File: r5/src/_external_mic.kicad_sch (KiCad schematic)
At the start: 132 parts, among them Q12 BSS84PW, Q13 BSS84PW, Q14 NX3008NBKW, Q15 NX3008NBKW, Q16 NX3008NBKW, Q17 NX3008NBKW, Q18 NX3008NBKW, Q19 NX3008NBKW, Q20 BSS84PW, Q21 BSS84PW, Q22 NX3008NBKW, Q23 NX3008NBKW, Q24 NX3008NBKW, Q25 BSS84PW, T18 , T19 , T20 , T23 , T24 , T25 , T26 , T27 , T28 , T29 , T30 , T31 , T32 , T33 , T34 , T35 , T37 , T38 , T43 , T44 , T45 , T46 , T47 , T48 , T49 , T50 , U17 74HC20, U18 THAT5173, U19 74HC74, U20 74HC132, U21 74HC4520, U22 74HC132, U23 THAT1580, U24 74HC688, U25 LM4562, U26 74HC688, U27 AD4005

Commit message: Updates to +/-15V supply. Additional output capacitance. Change to smaller inductor packages. Add 0R links to permit isolation of output. Mods to compensation network. Set feedback resistors to datasheet values.
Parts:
- renumbered C57 to C100, C82 to C101, C52 to C102, C27 to C103, C46 to C104, C47 to C105, C49 to C106, C50 to C107, C60 to C108, C54 to C109, C55 to C110, C84 to C111, C56 to C112, C58 to C113, C59 to C114, C62 to C115, C63 to C116, C64 to C117, C66 to C118, C65 to C119, C67 to C120, C68 to C121, C69 to C122, C70 to C123, C71 to C124, C72 to C125, C73 to C126, C74 to C127, C75 to C128, C76 to C129, C77 to C130, C78 to C131, C79 to C132, C25 to C95, C48 to C96, C53 to C97, C83 to C98, C81 to C99, D15 to D19, D8 to D20, D10 to D21, D11 to D22, D12 to D23, D14 to D24, D13 to D25, Q17 to Q14, Q18 to Q15, Q19 to Q16, Q20 to Q17, Q21 to Q18, Q15 to Q19, Q16 to Q20, Q14 to Q21, Q12 to Q22, Q13 to Q23, Q22 to Q24, Q23 to Q25, Q24 to Q26, Q25 to Q27, R71 to R100, R100 to R101, R79 to R67, R82 to R68, R84 to R69, R85 to R70, R73 to R71, R68 to R72, R74 to R73, R65 to R74, R72 to R75, R64 to R76, R66 to R77, R67 to R78, R47 to R79, R48 to R80, R49 to R82, R50 to R83, R51 to R84, R52 to R85, R55 to R87, R53 to R88, R54 to R89, R56 to R90, R57 to R91, R58 to R92, R59 to R93, R60 to R94, R61 to R95, R62 to R96, R63 to R97, R70 to R98, R69 to R99, T20 to T26, T19 to T27, T18 to T28, T37 to T29, T38 to T30, T44 to T31, T45 to T32, T46 to T33, T23 to T34, T24 to T35, T47 to T36, T43 to T37, T25 to T38, T26 to T39, T48 to T40, T27 to T41, T28 to T42, T29 to T43, T30 to T44, T31 to T45, T49 to T46, T32 to T47, T33 to T48, T50 to T49, T35 to T50, T34 to T51, U17 to U25, U19 to U26, U20 to U27, U22 to U28, U18 to U29, U21 to U30, U23 to U31, U24 to U32, U25 to U33, U26 to U34, U27 to U35

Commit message: Fix broken component annotation by importing back from PCB and fixing duplicates.
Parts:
- Q14: renamed from Q21; value NX3008NBKW -> NX6008NBKW
- renumbered C95 to C25, C103 to C27, C104 to C46, C105 to C47, C96 to C48, C106 to C49, C107 to C50, C102 to C52, C97 to C53, C109 to C54, C110 to C55, C112 to C56, C100 to C57, C113 to C58, C114 to C59, C108 to C60, C115 to C62, C116 to C63, C117 to C64, C119 to C65, C118 to C66, C120 to C67, C121 to C68, C122 to C69, C123 to C70, C124 to C71, C125 to C72, C126 to C73, C127 to C74, C128 to C75, C129 to C76, C130 to C77, C131 to C78, C132 to C79, C99 to C81, C101 to C82, C98 to C83, C111 to C84, D21 to D10, D22 to D11, D23 to D12, D25 to D13, D24 to D14, D19 to D15, D20 to D8, Q22 to Q12, Q23 to Q13, Q19 to Q15, Q20 to Q16, Q14 to Q17, Q15 to Q18, Q16 to Q19, Q17 to Q20, Q18 to Q21, Q24 to Q22, Q25 to Q23, Q26 to Q24, Q27 to Q25, R101 to R100, R79 to R47, R80 to R48, R82 to R49, R83 to R50, R84 to R51, R85 to R52, R88 to R53, R89 to R54, R87 to R55, R90 to R56, R91 to R57, R92 to R58, R93 to R59, R94 to R60, R95 to R61, R96 to R62, R97 to R63, R76 to R64, R74 to R65, R77 to R66, R78 to R67, R72 to R68, R99 to R69, R98 to R70, R100 to R71, R75 to R72, R71 to R73, R73 to R74, R67 to R79, R68 to R82, R69 to R84, R70 to R85, T28 to T18, T27 to T19, T26 to T20, T34 to T23, T35 to T24, T38 to T25, T39 to T26, T41 to T27, T42 to T28, T43 to T29, T44 to T30, T45 to T31, T47 to T32, T48 to T33, T51 to T34, T50 to T35, T29 to T37, T30 to T38, T37 to T43, T31 to T44, T32 to T45, T33 to T46, T36 to T47, T40 to T48, T46 to T49, T49 to T50, U25 to U17, U29 to U18, U26 to U19, U27 to U20, U30 to U21, U28 to U22, U31 to U23, U32 to U24, U33 to U25, U34 to U26, U35 to U27

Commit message: Add reverse-blocking diodes to prevent P48V current flowing into +3.3VA
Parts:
- added D26, D27: 1SS387, Diode_SMD:D_SOD-523, symbol Device:D
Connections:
- net MIC_IN_N: now also D26.1 (K); no longer R84.1
- net MIC_IN_P: now also D27.1 (K); no longer R85.1
- new net: D26.2 (A), R84.1
- new net: D27.2 (A), R85.1
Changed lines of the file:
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@@
     (stroke (width 0) (type default))
   )
+  (wire (pts (xy 123.19 260.35) (xy 123.19 318.77))
+    (stroke (width 0) (type default))
+  )
   (wire (pts (xy 340.36 270.51) (xy 340.36 269.24))
     (stroke (width 0) (type default))
@@
     (stroke (width 0) (type default))
   )
-  (wire (pts (xy 113.03 250.19) (xy 113.03 351.79))
+  (wire (pts (xy 113.03 250.19) (xy 113.03 252.73))
     (stroke (width 0) (type default))
   )
@@
     (stroke (width 0) (type default))
   )
+  (wire (pts (xy 113.03 260.35) (xy 113.03 351.79))
+    (stroke (width 0) (type default))
+  )
   (wire (pts (xy 350.52 332.74) (xy 368.3 332.74))
     (stroke (width 0) (type default))
@@
     (stroke (width 0) (type default))
   )
-  (wire (pts (xy 123.19 250.19) (xy 123.19 318.77))
+  (wire (pts (xy 123.19 250.19) (xy 123.19 252.73))
     (stroke (width 0) (type default))
   )
@@
     )
   )
+  (symbol (lib_id "Device:D") (at 113.03 256.54 90) (unit 1)
+    (in_bom yes) (on_board yes) (dnp no)
+    (property "Reference" "D26" (at 115.57 256.54 0)
+      (effects (font (size 1.27 1.27)) (justify right))
+    )
+    (property "Value" "1SS387" (at 118.11 252.73 0)
+      (effects (font (size 1.27 1.27)) (justify right))
+    )
+    (property "Footprint" "Diode_SMD:D_SOD-523" (at 113.03 256.54 0)
+      (effects (font (size 1.27 1.27)) hide)
+    )
+    (property "Datasheet" "~" (at 113.03 256.54 0)
+      (effects (font (size 1.27 1.27)) hide)
+    )
+    (pin "1")
+    (pin "2")
+    (instances
+      (project "bugg-main-r5"
+        (path "/e3eb514f-6ce4-4abe-ba20-f82f0015628f/41f15edd-4583-4f5d-8a81-daeb7c83b416"
+          (reference "D26") (unit 1)
+        )
+      )
+    )
+  )
   (symbol (lib_id "power:GNDA") (at 405.13 276.86 270) (unit 1)
     (in_bom yes) (on_board yes) (dnp no)
@@
         )
       )
+    )
+  )
+  (symbol (lib_id "Device:D") (at 123.19 256.54 90) (unit 1)
+    (in_bom yes) (on_board yes) (dnp no)
+    (property "Reference" "D27" (at 125.73 256.54 0)
+      (effects (font (size 1.27 1.27)) (justify right))
+    )
+    (property "Value" "1SS387" (at 128.27 252.73 0)
+      (effects (font (size 1.27 1.27)) (justify right))
+    )
+    (property "Footprint" "Diode_SMD:D_SOD-523" (at 123.19 256.54 0)
+      (effects (font (size 1.27 1.27)) hide)
+    )
+    (property "Datasheet" "~" (at 123.19 256.54 0)
+      (effects (font (size 1.27 1.27)) hide)
+    )
+    (pin "1")
+    (pin "2")
+    (instances
+      (project "bugg-main-r5"
+        (path "/e3eb514f-6ce4-4abe-ba20-f82f0015628f/41f15edd-4583-4f5d-8a81-daeb7c83b416"
+          (reference "D27") (unit 1)
+        )
+      )

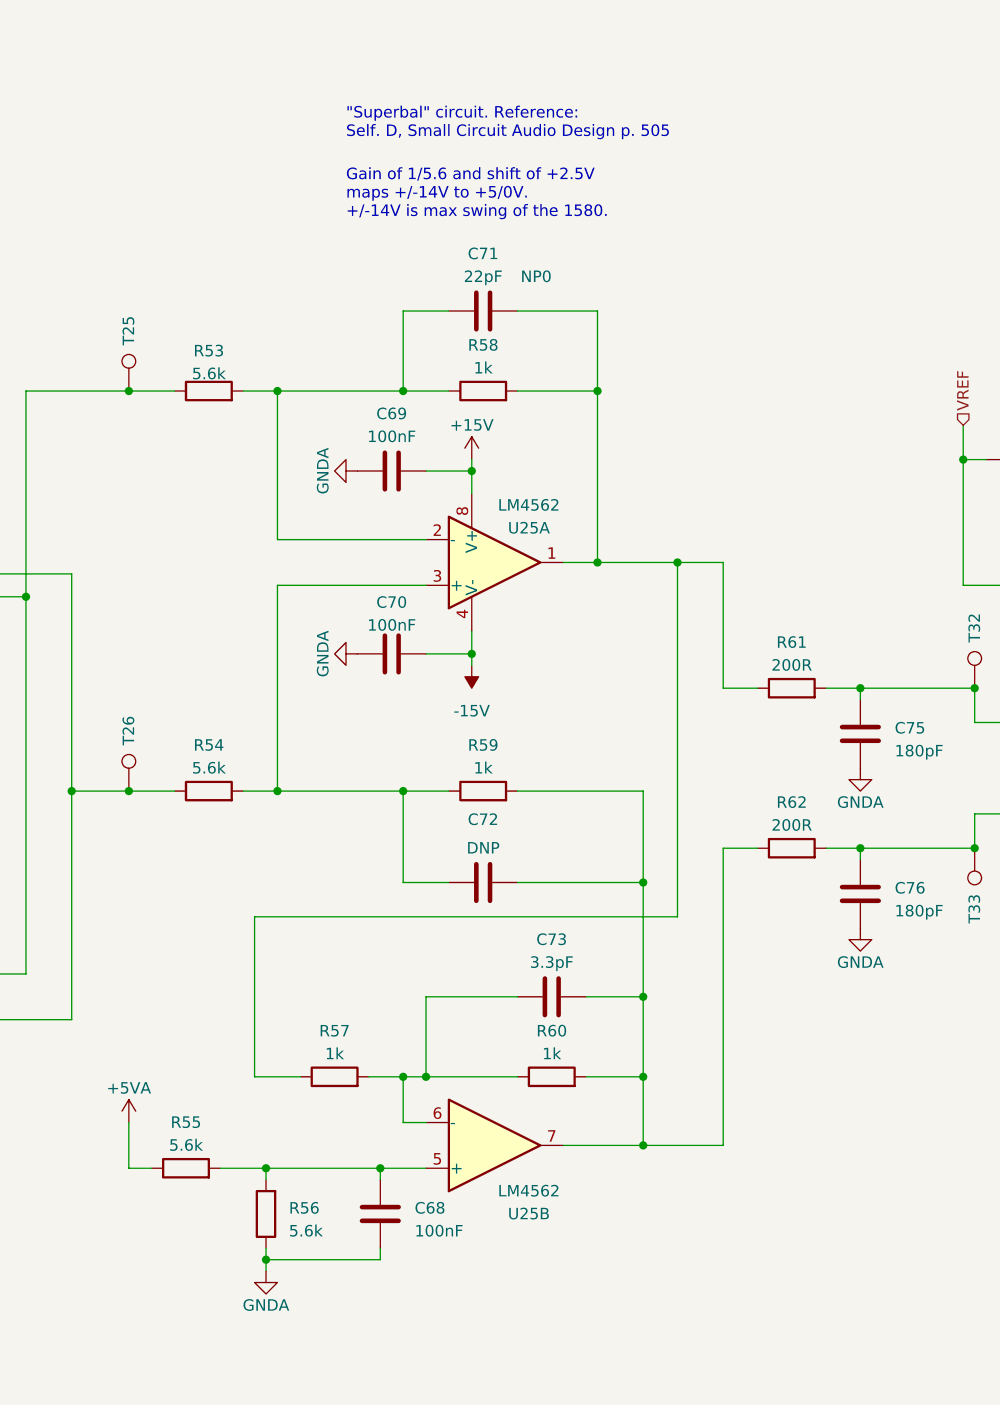
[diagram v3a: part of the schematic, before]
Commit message: Increase gain of Superbal ADC driver
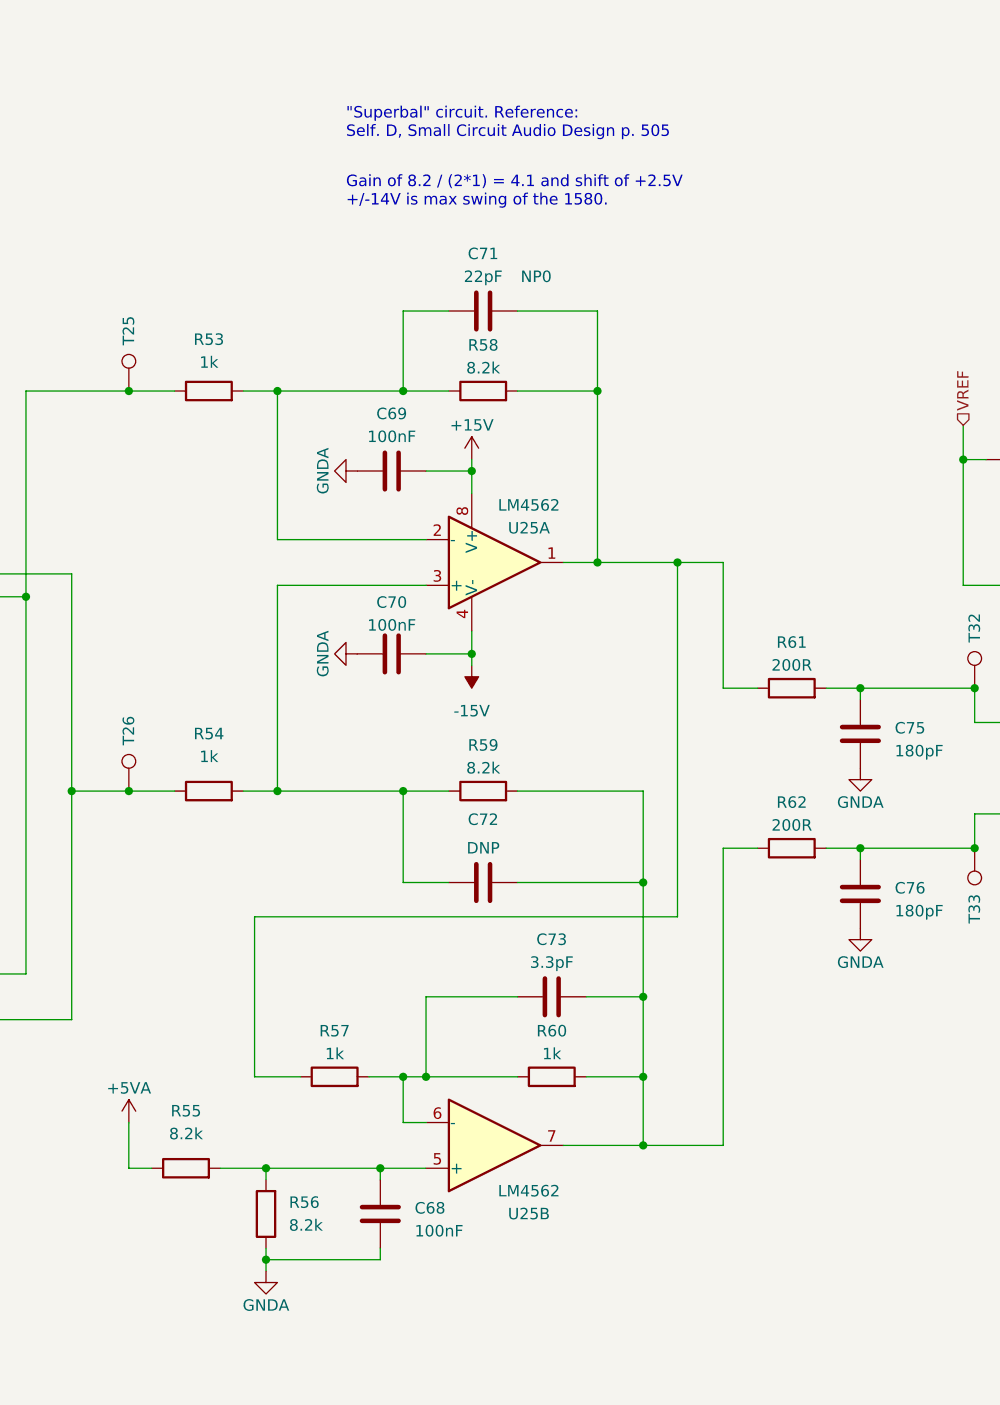
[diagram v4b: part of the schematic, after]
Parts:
- R53, R54: value 5.6k -> 1k
- R55, R56: value 5.6k -> 8.2k
- R58, R59: value 1k -> 8.2k
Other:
- note added: "Gain of 8.2 / (2*1) = 4.1 and shift of +2.5V +/-14V is max swing of the 1580."
- note removed: "Gain of 1/5.6 and shift of +2.5V maps +/-14V to +5/0V. +/-14V is max swing of the 1580."
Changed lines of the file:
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@@
     (effects (font (size 1.27 1.27)) (justify left bottom))
   )
-  (text "Gain of 1/5.6 and shift of +2.5V\nmaps +/-14V to +5/0V.\n+/-14V is max swing of the 1580." (exclude_from_sim no)
-    (at 403.86 248.92 0)
+  (text "Gain of 8.2 / (2*1) = 4.1 and shift of +2.5V\n+/-14V is max swing of the 1580." (exclude_from_sim no)
+    (at 403.86 247.65 0)
     (effects (font (size 1.27 1.27)) (justify left bottom))
   )
@@
   )
   (symbol (lib_id "Device:R") (at 419.1 312.42 90) (unit 1)
-    (in_bom yes) (on_board yes) (dnp no) (fields_autoplaced)
+    (in_bom yes) (on_board yes) (dnp no)
     (property "Reference" "R59" (at 419.1 307.34 90)
       (effects (font (size 1.27 1.27)))
     )
-    (property "Value" "1k" (at 419.1 309.88 90)
+    (property "Value" "8.2k" (at 419.1 309.88 90)
       (effects (font (size 1.27 1.27)))
     )
@@
   )
   (symbol (lib_id "Device:R") (at 419.1 267.97 90) (unit 1)
-    (in_bom yes) (on_board yes) (dnp no) (fields_autoplaced)
+    (in_bom yes) (on_board yes) (dnp no)
     (property "Reference" "R58" (at 419.1 262.89 90)
       (effects (font (size 1.27 1.27)))
     )
-    (property "Value" "1k" (at 419.1 265.43 90)
+    (property "Value" "8.2k" (at 419.1 265.43 90)
       (effects (font (size 1.27 1.27)))
     )
@@
   (symbol (lib_id "Device:R") (at 386.08 354.33 90) (unit 1)
     (in_bom yes) (on_board yes) (dnp no) (fields_autoplaced)
-    (property "Reference" "R55" (at 386.08 349.25 90)
+    (property "Reference" "R55" (at 386.08 347.98 90)
       (effects (font (size 1.27 1.27)))
     )
-    (property "Value" "5.6k" (at 386.08 351.79 90)
+    (property "Value" "8.2k" (at 386.08 350.52 90)
       (effects (font (size 1.27 1.27)))
     )
@@
   (symbol (lib_id "Device:R") (at 394.97 359.41 180) (unit 1)
     (in_bom yes) (on_board yes) (dnp no) (fields_autoplaced)
-    (property "Reference" "R56" (at 397.51 358.775 0)
+    (property "Reference" "R56" (at 397.51 358.14 0)
       (effects (font (size 1.27 1.27)) (justify right))
     )
-    (property "Value" "5.6k" (at 397.51 361.315 0)
+    (property "Value" "8.2k" (at 397.51 360.68 0)
       (effects (font (size 1.27 1.27)) (justify right))
     )
@@
   (symbol (lib_id "Device:R") (at 388.62 267.97 90) (unit 1)
     (in_bom yes) (on_board yes) (dnp no)
-    (property "Reference" "R53" (at 388.62 263.525 90)
+    (property "Reference" "R53" (at 388.62 262.255 90)
       (effects (font (size 1.27 1.27)))
     )
-    (property "Value" "5.6k" (at 388.62 266.065 90)
+    (property "Value" "1k" (at 388.62 264.795 90)
       (effects (font (size 1.27 1.27)))
     )
@@
   )
   (symbol (lib_id "Device:R") (at 388.62 312.42 90) (unit 1)
-    (in_bom yes) (on_board yes) (dnp no) (fields_autoplaced)
-    (property "Reference" "R54" (at 388.62 307.34 90)
+    (in_bom yes) (on_board yes) (dnp no)
+    (property "Reference" "R54" (at 388.62 306.07 90)
       (effects (font (size 1.27 1.27)))
     )
-    (property "Value" "5.6k" (at 388.62 309.88 90)
+    (property "Value" "1k" (at 388.62 308.61 90)
       (effects (font (size 1.27 1.27)))
     )

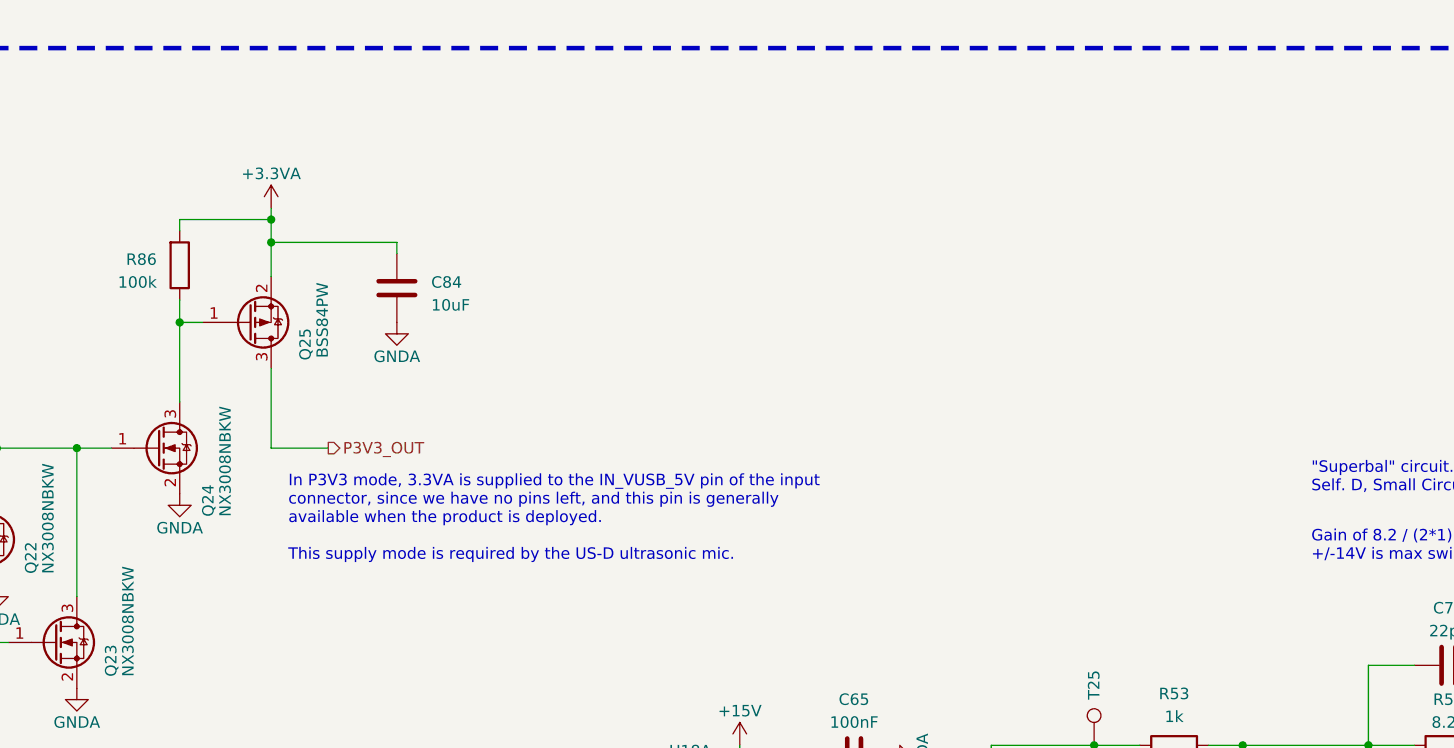
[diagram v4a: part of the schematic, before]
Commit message: Change P3V3 phantom supply p-FETs to lower-Rdson type (same as 15V DCDC input FET
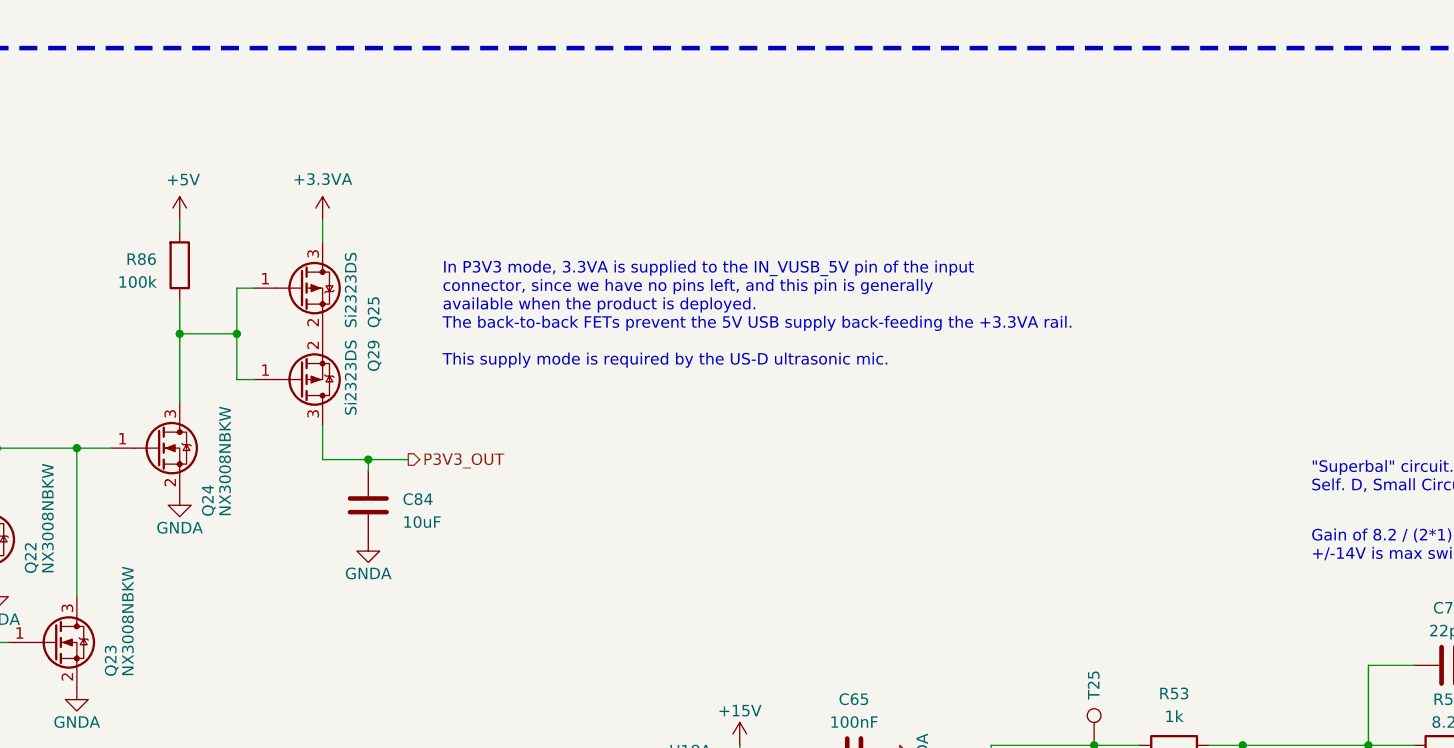
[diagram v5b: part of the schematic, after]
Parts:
- added Q29: Si2323DS, Package_TO_SOT_SMD:SOT-23, symbol Device:Q_PMOS_GSD
- Q25: value BSS84PW -> Si2323DS; footprint Package_TO_SOT_SMD:SOT-323_SC-70 -> Package_TO_SOT_SMD:SOT-23
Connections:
- net +3.3VA: now also Q25.3 (D); no longer C84.2, Q25.2 (S), R86.2
- net P3V3_OUT: now also C84.2, Q29.3 (D); no longer Q25.3 (D)
- net at Q24.3 (D), Q25.1 (G), R86.1: now also Q29.1 (G)
- new net: Q25.2 (S), Q29.2 (S)
- new net +5V: R86.2
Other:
- note added: "In P3V3 mode, 3.3VA is supplied to the IN_VUSB_5V pin of the input connector, since we have no pins left, and this pin is generally available when the product is deployed. The back-to-back FETs prevent the 5V USB supply back-feeding the +3.3VA rail. This supply mode is required by the US-D ultrasonic mic."
- note removed: "In P3V3 mode, 3.3VA is supplied to the IN_VUSB_5V pin of the input connector, since we have no pins left, and this pin is generally available when the product is deployed. This supply mode is required by the US-D ultrasonic mic."
- moved on the sheet: C84

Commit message: Add voltage supervisor to detect 5V USB presence and force P3V3 phantom to be disabled even if it's selected
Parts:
- added Q30: NX3008NBKW, Package_TO_SOT_SMD:SOT-323_SC-70, symbol Device:Q_NMOS_GSD
- added R80: 1k, Resistor_SMD:R_0402_1005Metric, symbol Device:R
- added T59: (no value), TestPoint:TestPoint_Pad_D1.0mm, symbol Connector:TestPoint
- added U36: APX809S-40SA, Package_TO_SOT_SMD:SOT-23, symbol j_Power_Management:APX809S-xxSA
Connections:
- net GNDA: now also Q30.2 (S), R80.2, U36.1 (GND)
- net P3V3_OUT: now also U36.3 (VCC)
- net at Q22.3 (D), Q23.3 (D), Q24.1 (G)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: now also Q30.3 (D)
- new net: Q30.1 (G), R80.1, T59.1, U36.2 (~{RESET})
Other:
- note added: "In P3V3 mode, 3.3VA is supplied to the IN_VUSB_5V pin of the input connector, since we have no pins left, and this pin is generally available when the product is deployed. The back-to-back FETs prevent the 5V USB supply back-feeding the +3.3VA rail. U36 detects 5V USB presence and disables 3.3V phantom even if P3V3_EN is asserted. This supply mode is required by the US-D ultrasonic mic."
- note removed: "In P3V3 mode, 3.3VA is supplied to the IN_VUSB_5V pin of the input connector, since we have no pins left, and this pin is generally available when the product is deployed. The back-to-back FETs prevent the 5V USB supply back-feeding the +3.3VA rail. This supply mode is required by the US-D ultrasonic mic."
- moved on the sheet: C27, C46, C47, C49, C50, C54, C55, C56, C58, C59, C62, C63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
